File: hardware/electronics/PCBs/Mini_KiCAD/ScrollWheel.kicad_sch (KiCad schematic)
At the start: 7 parts

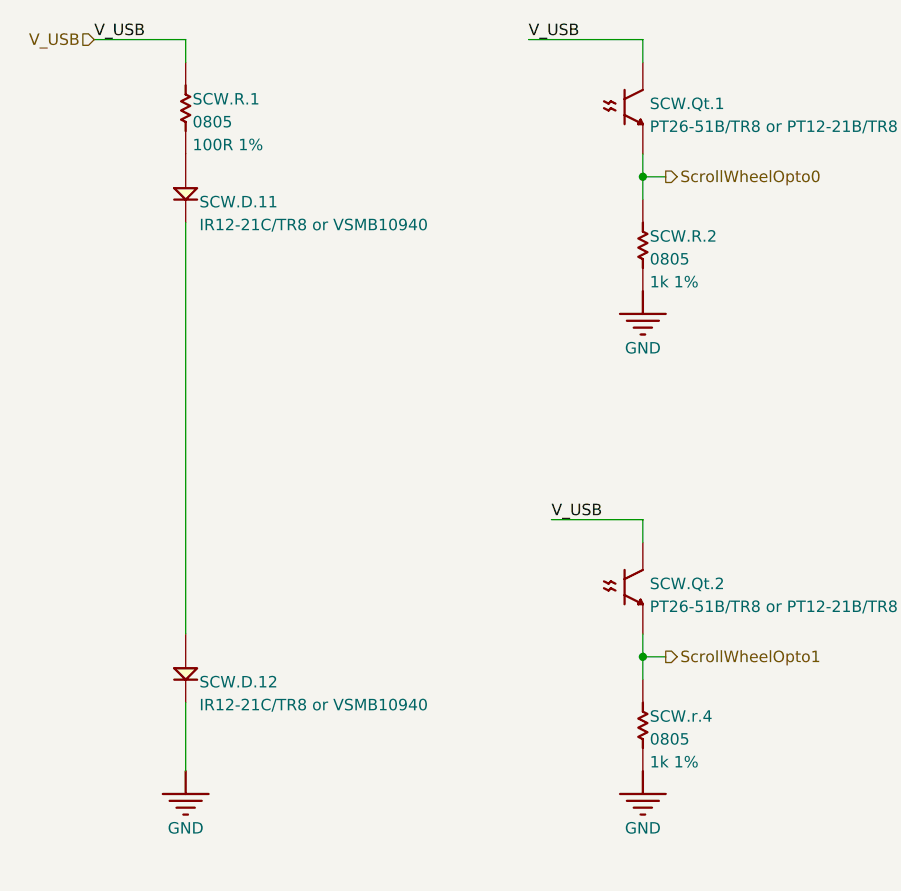
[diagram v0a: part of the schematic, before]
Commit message: Initial commit of the PCB project file replacing the ADNS-5050 with PMW3360, referencing the schematic of the Ploopy Classic.
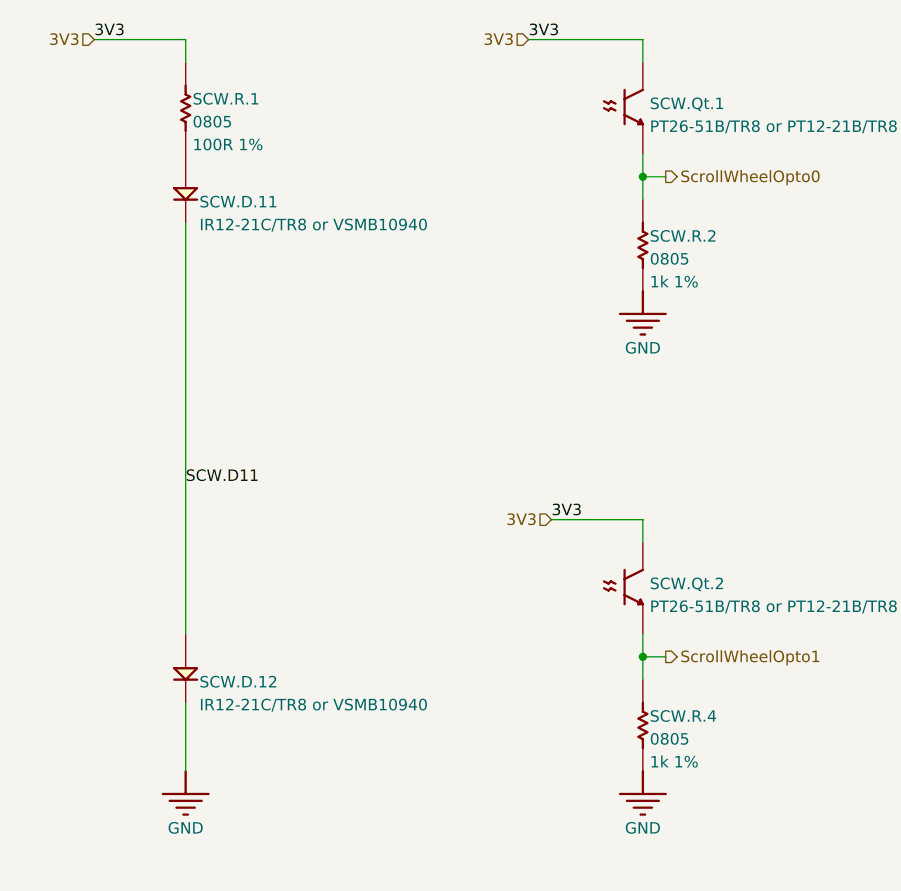
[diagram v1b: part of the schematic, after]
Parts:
- SCW.D.11, SCW.D.12: footprint IR12-21C/TR8 -> LEDs:XZTHI56W-1
- SCW.Qt.1, SCW.Qt.2: footprint PT26-51B/TR8 -> OptoElectronics.PcbLib:PT26-51B_TR8
- SCW.R.1, SCW.R.2: footprint 0805 -> Chip_Passives.PcbLib:0805
- SCW.R.4: renamed from SCW.r.4; footprint 0805 -> Chip_Passives.PcbLib:0805
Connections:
- net SCW.D11: now reaches SCW.D.11.C, SCW.D.12.A
- net V_USB renamed 3V3
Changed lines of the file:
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@@
 		)
 	)
-	(label "V_USB"
+	(label "3V3"
 		(at 91.44 60.96 0)
 		(fields_autoplaced yes)
@@
 		)
 	)
-	(label "V_USB"
-		(at 142.24 114.3 0)
+	(label "SCW.D11"
+		(at 101.6 110.49 0)
 		(fields_autoplaced yes)
 		(effects
@@
 		)
 	)
-	(label "V_USB"
+	(label "3V3"
 		(at 139.7 60.96 0)
+		(fields_autoplaced yes)
+		(effects
+			(font
+				(size 1.27 1.27)
+			)
+			(justify left bottom)
+		)
+	)
+	(label "3V3"
+		(at 142.24 114.3 0)
 		(fields_autoplaced yes)
 		(effects
@@
 		)
 	)
+	(hierarchical_label "3V3"
+		(shape input)
+		(at 142.24 114.3 180)
+		(fields_autoplaced yes)
+		(effects
+			(font
+				(size 1.27 1.27)
+			)
+			(justify right)
+		)
+	)
 	(hierarchical_label "ScrollWheelOpto1"
 		(shape output)
@@
 		)
 	)
-	(hierarchical_label "V_USB"
+	(hierarchical_label "3V3"
+		(shape input)
+		(at 139.7 60.96 180)
+		(fields_autoplaced yes)
+		(effects
+			(font
+				(size 1.27 1.27)
+			)
+			(justify right)
+		)
+	)
+	(hierarchical_label "3V3"
 		(shape input)
 		(at 91.44 60.96 180)
@@
 		(on_board yes)
 		(dnp no)
-		(property "Reference" "SCW.r.4"
+		(property "Reference" "SCW.R.4"
 			(at 153.162 136.906 0)
 			(effects
@@
 			)
 		)
-		(property "Footprint" "0805"
+		(property "Footprint" "Chip_Passives.PcbLib:0805"
 			(at 149.86 139.7 0)
 			(effects
@@
 			(project "Mini"
 				(path "/4010ea29-f248-4f19-83ee-6b19cd4442a4/10daec88-f6fe-4771-a75f-0b8234f02ca1"
-					(reference "SCW.r.4")
+					(reference "SCW.R.4")
 					(unit 1)
 				)
@@
 			)
 		)
-		(property "Footprint" "PT26-51B/TR8"
+		(property "Footprint" "OptoElectronics.PcbLib:PT26-51B_TR8"
 			(at 152.4 124.46 0)
 			(effects
@@
 			)
 		)
-		(property "Footprint" "IR12-21C/TR8"
+		(property "Footprint" "LEDs:XZTHI56W-1"
 			(at 101.6 78.74 0)
 			(effects
@@
 			)
 		)
-		(property "Footprint" "0805"
+		(property "Footprint" "Chip_Passives.PcbLib:0805"
 			(at 149.86 86.36 0)
 			(effects
@@
 			)
 		)
-		(property "Footprint" "0805"
+		(property "Footprint" "Chip_Passives.PcbLib:0805"
 			(at 99.06 71.12 0)
 			(effects
@@
 			)
 		)
-		(property "Footprint" "PT26-51B/TR8"
+		(property "Footprint" "OptoElectronics.PcbLib:PT26-51B_TR8"
 			(at 152.4 71.12 0)
 			(effects
@@
 			)
 		)
-		(property "Footprint" "IR12-21C/TR8"
+		(property "Footprint" "LEDs:XZTHI56W-1"
 			(at 101.6 132.08 0)
 			(effects
